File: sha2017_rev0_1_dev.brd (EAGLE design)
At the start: 65 x 80 mm, 87 parts, among them IC1 AP7215, IC2 LM1117, IC3 CP210X_USB_UART, IC4 ESP32WROOM32, Q1 MMBT2222A, Q2 MMBT2222A, Q3 SI1304 BDL, SW100 MCMT5-F-V, X701 2908-05WB-MG

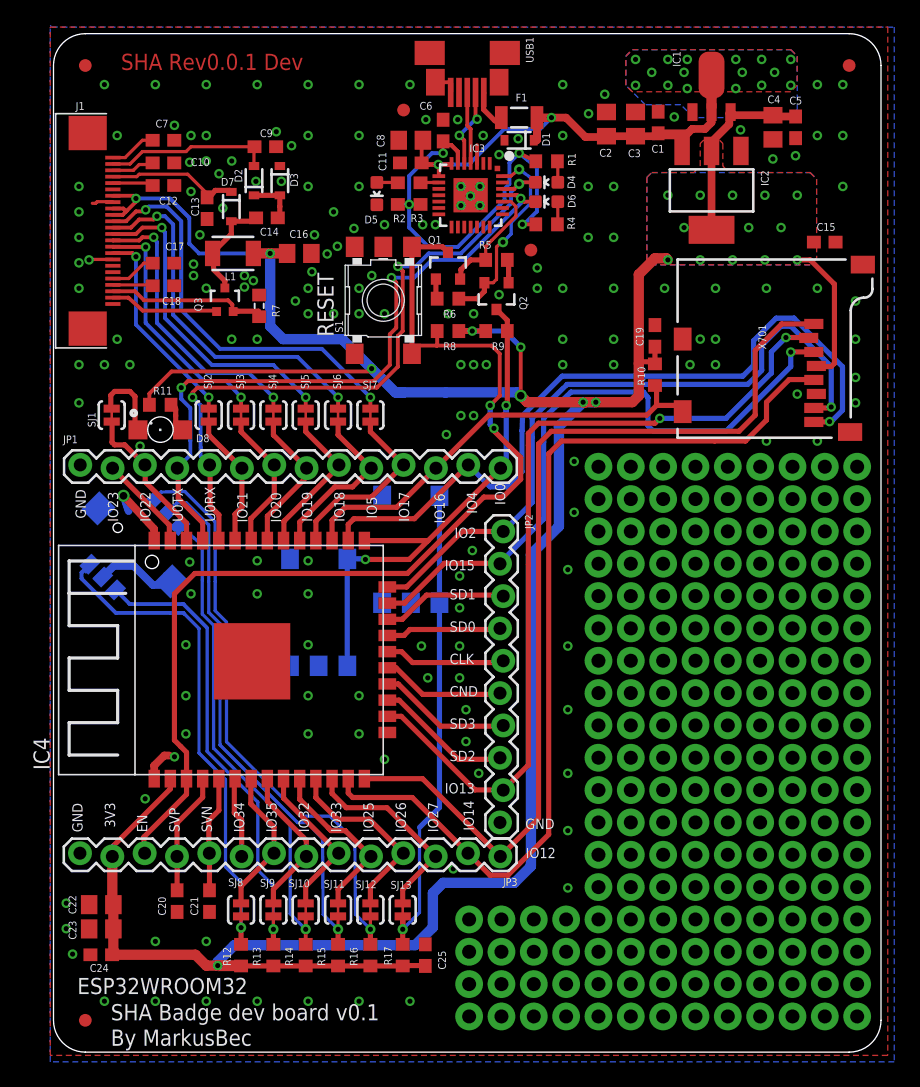
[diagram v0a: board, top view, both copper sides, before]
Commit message: added markings
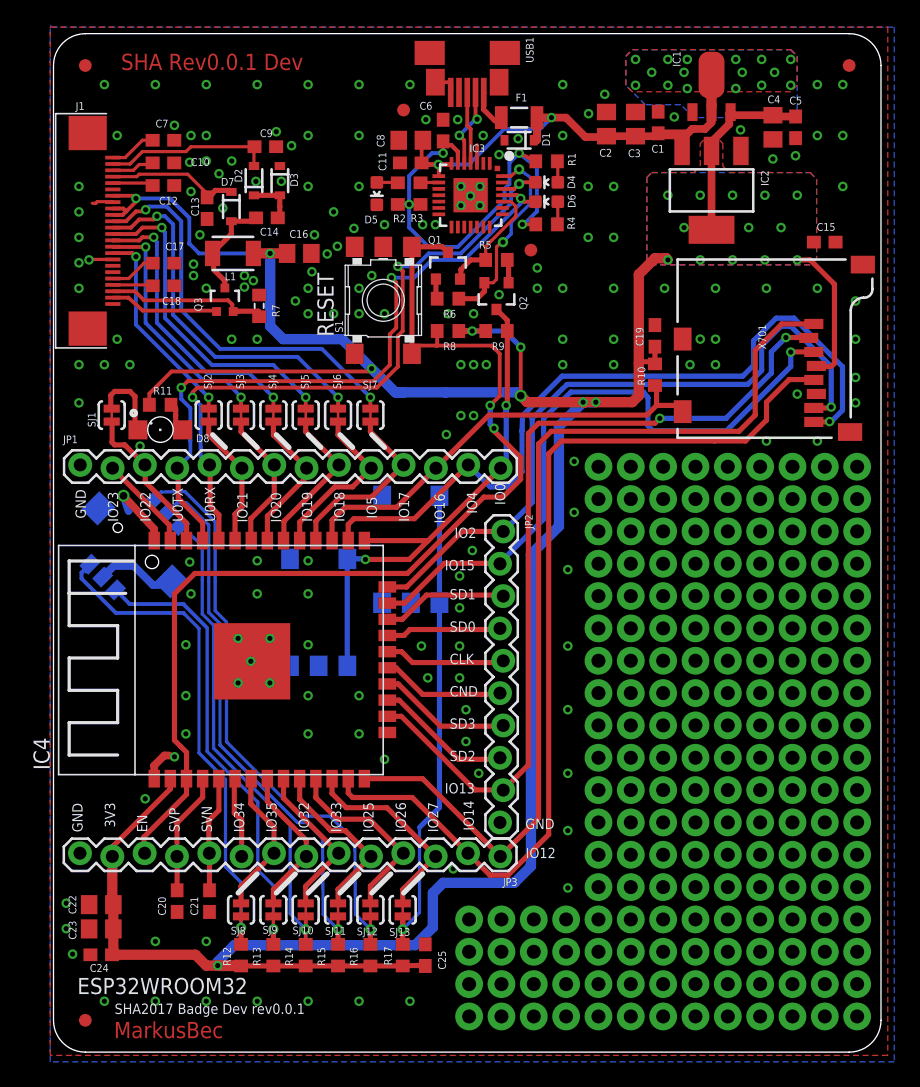
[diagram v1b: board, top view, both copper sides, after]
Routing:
- net GND: vias 171 -> 176
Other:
- board text added: "MarkusBec"
- board text added: "SHA2017 Badge Dev rev0.0.1"
- board text removed: "By MarkusBec"
- board text removed: "SHA Badge dev board v0.1"
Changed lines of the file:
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@@
 <?xml version="1.0" encoding="utf-8"?>
 <!DOCTYPE eagle SYSTEM "eagle.dtd">
-<eagle version="7.2.0">
+<eagle version="6.6.0">
 <drawing>
 <settings>
@@
 <setting verticaltext="up"/>
 </settings>
-<grid distance="0.5" unitdist="mm" unit="mm" style="lines" multiple="1" display="yes" altdistance="0.025" altunitdist="inch" altunit="inch"/>
+<grid distance="0.1" unitdist="mm" unit="mm" style="lines" multiple="1" display="yes" altdistance="0.025" altunitdist="inch" altunit="inch"/>
 <layers>
 <layer number="1" name="Top" color="4" fill="1" visible="yes" active="yes"/>
@@
 <layer number="60" name="bCarbon" color="7" fill="1" visible="no" active="no"/>
 <layer number="61" name="stand" color="7" fill="1" visible="no" active="no"/>
-<layer number="90" name="Modules" color="5" fill="1" visible="no" active="no"/>
+<layer number="90" name="Modules" color="5" fill="1" visible="no" active="yes"/>
 <layer number="91" name="Nets" color="2" fill="1" visible="no" active="no"/>
 <layer number="92" name="Busses" color="1" fill="1" visible="no" active="no"/>
@@
 <wire x1="2.5" y1="80" x2="0" y2="77.5" width="0" layer="20" curve="90"/>
 <wire x1="1.524" y1="50.038" x2="1.524" y2="79.248" width="0.4064" layer="22"/>
-<wire x1="1.524" y1="79.248" x2="63.246" y2="79.248" width="0.4064" layer="22"/>
-<wire x1="63.246" y1="79.248" x2="63.246" y2="50.038" width="0.4064" layer="22"/>
+<wire x1="1.524" y1="79.248" x2="9.906" y2="79.248" width="0.4064" layer="22"/>
+<wire x1="9.906" y1="79.248" x2="63.246" y2="79.248" width="0.4064" layer="22"/>
+<wire x1="63.246" y1="79.248" x2="63.246" y2="55.626" width="0.4064" layer="22"/>
+<wire x1="63.246" y1="55.626" x2="63.246" y2="50.038" width="0.4064" layer="22"/>
 <wire x1="63.246" y1="50.038" x2="1.524" y2="50.038" width="0.4064" layer="22"/>
 <polygon width="0.3048" layer="42">
@@
 <vertex x="0.127" y="17.018"/>
 </polygon>
-<text x="5.3" y="77.15" size="1.27" layer="1" font="vector" ratio="12">SHA Rev0.0.1 Dev</text>
+<text x="5.3" y="77.15" size="1.27" layer="1" font="vector" ratio="15">SHA Rev0.0.1 Dev</text>
+<text x="4.75" y="1.1" size="1.27" layer="1" font="vector" ratio="15">MarkusBec</text>
 <text x="2.286" y="17.272" size="0.8128" layer="25" font="vector" ratio="12" rot="R90">GND</text>
 <text x="7.366" y="17.272" size="0.8128" layer="25" font="vector" ratio="12" rot="R90">EN</text>
@@
 <text x="21.3" y="38.2" size="1.27" layer="26" font="vector" ratio="11" rot="MR0">A</text>
 <text x="24.6" y="34.6" size="0.6096" layer="26" font="vector" ratio="11" rot="MR270">FLASH</text>
-<text x="4.5" y="2.5" size="1.27" layer="25" font="vector" ratio="10">SHA Badge dev board v0.1</text>
-<text x="4.5" y="0.5" size="1.27" layer="25" font="vector" ratio="10">By MarkusBec</text>
+<wire x1="12.5" y1="48.5" x2="13.5" y2="47.5" width="0.4064" layer="25"/>
+<wire x1="15" y1="48.5" x2="16" y2="47.5" width="0.4064" layer="25"/>
+<wire x1="17.5" y1="48.5" x2="18.5" y2="47.5" width="0.4064" layer="25"/>
+<wire x1="20" y1="48.5" x2="21" y2="47.5" width="0.4064" layer="25"/>
+<wire x1="22.5" y1="48.5" x2="23.5" y2="47.5" width="0.4064" layer="25"/>
+<wire x1="25" y1="48.5" x2="26" y2="47.5" width="0.4064" layer="25"/>
+<wire x1="14.5" y1="12.5" x2="16" y2="14" width="0.4064" layer="25"/>
+<wire x1="17.5" y1="12.5" x2="19" y2="14" width="0.4064" layer="25"/>
+<wire x1="20" y1="12.5" x2="21.5" y2="14" width="0.4064" layer="25"/>
+<wire x1="22.5" y1="12.5" x2="24" y2="14" width="0.4064" layer="25"/>
+<wire x1="25" y1="12.5" x2="26.5" y2="14" width="0.4064" layer="25"/>
+<wire x1="27.5" y1="12.5" x2="29" y2="14" width="0.4064" layer="25"/>
+<text x="4.8" y="3" size="0.8128" layer="25" font="vector" ratio="15">SHA2017 Badge Dev rev0.0.1</text>
+<text x="4.75" y="1.1" size="1.27" layer="29" font="vector" ratio="15">MarkusBec</text>
 </plain>
 <attributes>
@@
 <pass name="Default">
 <param name="RoutingGrid" value="50mil"/>
-<param name="AutoGrid" value="1"/>
-<param name="Efforts" value="0"/>
-<param name="TopRouterVariant" value="1"/>
 <param name="tpViaShape" value="round"/>
 <param name="PrefDir.1" value="|"/>
@@
 </element>
 <element name="SJ8" library="SparkFun-Passives" package="PAD-JUMPER-2-NC_BY_TRACE_YES_SILK" value="JUMPER-PAD-2-NC_BY_TRACE" x="14.732" y="11.176" smashed="yes" rot="R90">
-<attribute name="NAME" x="13.7235" y="13.038" size="0.6096" layer="25" font="vector" ratio="12"/>
+<attribute name="NAME" x="13.9235" y="9.238" size="0.6096" layer="25" font="vector" ratio="12"/>
 <attribute name="VALUE" x="16.383" y="10.2235" size="0.4064" layer="27" rot="R90"/>
 </element>
 <element name="SJ9" library="SparkFun-Passives" package="PAD-JUMPER-2-NC_BY_TRACE_YES_SILK" value="JUMPER-PAD-2-NC_BY_TRACE" x="17.272" y="11.176" smashed="yes" rot="R90">
-<attribute name="NAME" x="16.2235" y="12.998" size="0.6096" layer="25" font="vector" ratio="12"/>
+<attribute name="NAME" x="16.4235" y="9.298" size="0.6096" layer="25" font="vector" ratio="12"/>
 <attribute name="VALUE" x="18.923" y="10.2235" size="0.4064" layer="27" rot="R90"/>
 </element>
 <element name="SJ10" library="SparkFun-Passives" package="PAD-JUMPER-2-NC_BY_TRACE_YES_SILK" value="JUMPER-PAD-2-NC_BY_TRACE" x="19.812" y="11.176" smashed="yes" rot="R90">
-<attribute name="NAME" x="18.4735" y="12.958" size="0.6096" layer="25" font="vector" ratio="12"/>
+<attribute name="NAME" x="18.7735" y="9.258" size="0.6096" layer="25" font="vector" ratio="12"/>
 <attribute name="VALUE" x="21.463" y="10.2235" size="0.4064" layer="27" rot="R90"/>
 </element>
 <element name="SJ12" library="SparkFun-Passives" package="PAD-JUMPER-2-NC_BY_TRACE_YES_SILK" value="JUMPER-PAD-2-NC_BY_TRACE" x="24.892" y="11.176" smashed="yes" rot="R90">
-<attribute name="NAME" x="23.7235" y="12.878" size="0.6096" layer="25" font="vector" ratio="12"/>
+<attribute name="NAME" x="23.8235" y="9.178" size="0.6096" layer="25" font="vector" ratio="12"/>
 <attribute name="VALUE" x="26.543" y="10.2235" size="0.4064" layer="27" rot="R90"/>
 </element>
 <element name="SJ11" library="SparkFun-Passives" package="PAD-JUMPER-2-NC_BY_TRACE_YES_SILK" value="JUMPER-PAD-2-NC_BY_TRACE" x="22.352" y="11.176" smashed="yes" rot="R90">
-<attribute name="NAME" x="21.2235" y="12.918" size="0.6096" layer="25" font="vector" ratio="12"/>
+<attribute name="NAME" x="21.3235" y="9.218" size="0.6096" layer="25" font="vector" ratio="12"/>
 <attribute name="VALUE" x="24.003" y="10.2235" size="0.4064" layer="27" rot="R90"/>
 </element>
 <element name="SJ13" library="SparkFun-Passives" package="PAD-JUMPER-2-NC_BY_TRACE_YES_SILK" value="JUMPER-PAD-2-NC_BY_TRACE" x="27.432" y="11.176" smashed="yes" rot="R90">
-<attribute name="NAME" x="26.4735" y="12.838" size="0.6096" layer="25" font="vector" ratio="12"/>
+<attribute name="NAME" x="26.3735" y="9.138" size="0.6096" layer="25" font="vector" ratio="12"/>
 <attribute name="VALUE" x="29.083" y="10.2235" size="0.4064" layer="27" rot="R90"/>
 </element>
@@
 <attribute name="VALUE" x="54.102" y="57.15" size="0.8128" layer="27" rot="R270"/>
 <attribute name="PARTNO" value="2908-05WB-MG" x="49.022" y="48.26" size="1.778" layer="27" rot="R270" display="off"/>
+<variant name="PRODUCTION" populate="no"/>
 </element>
 <element name="R10" library="rcl" package="R0603" value="100k" x="47.244" y="53.213" smashed="yes" rot="R270">
@@
 <element name="IC4" library="ESP3x" package="ESP32MOD" value="ESP32WROOM32" x="27.9" y="20.8" smashed="yes" rot="R90">
 <attribute name="NAME" x="-0.3" y="22.16" size="1.27" layer="25" rot="R90"/>
-<attribute name="VALUE" x="1.87" y="4.56" size="1.27" layer="25" font="vector"/>
+<attribute name="VALUE" x="1.87" y="4.56" size="1.27" layer="25" font="vector" ratio="15"/>
 </element>
 <element name="JP2" library="SparkFun-Connectors" package="1X10_LOCK" value="M10LOCK" x="35.2" y="40.9" smashed="yes" rot="R270">
@@
 <via x="1" y="9.7" extent="1-16" drill="0.4" diameter="0.6096"/>
 <via x="1" y="11.7" extent="1-16" drill="0.4" diameter="0.6096"/>
+<via x="14.5" y="32.5" extent="1-16" drill="0.4" diameter="0.6096"/>
+<via x="17" y="32.5" extent="1-16" drill="0.4" diameter="0.6096"/>
+<via x="15.5" y="30.7" extent="1-16" drill="0.4" diameter="0.6096"/>
+<via x="14.5" y="29" extent="1-16" drill="0.4" diameter="0.6096"/>
+<via x="17" y="29" extent="1-16" drill="0.4" diameter="0.6096"/>
 </signal>
 <signal name="USB_DN_CON">

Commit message: Swapped NC and IO23
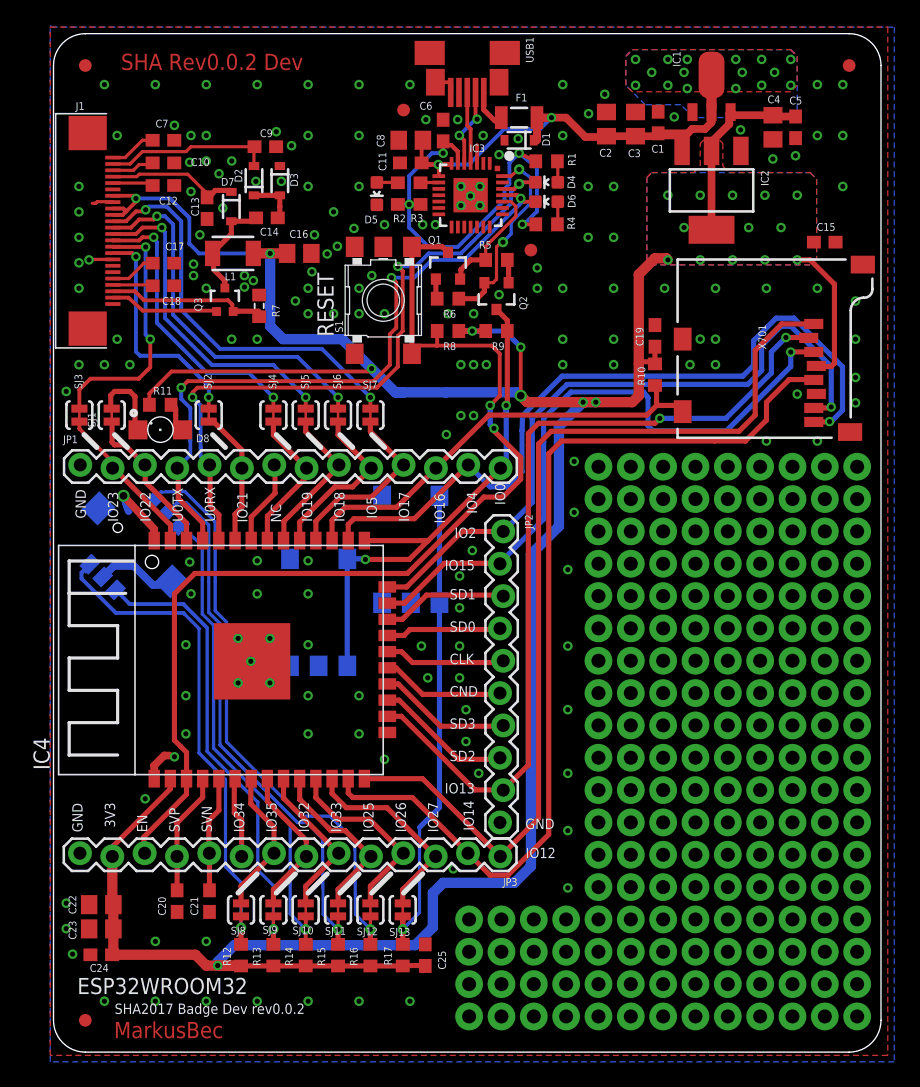
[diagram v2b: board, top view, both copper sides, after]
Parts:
- moved SJ3 12.7 mm to (2.03, 50.0)
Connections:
- removed net N$18: IC4.32, JP1.7, SJ3.1
- new net N$2: IC4.37, JP1.2, SJ3.1
- net N$15: now also IC4.32, JP1.7; no longer IC4.37, JP1.2
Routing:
- net N$2: track 0.00 -> 12.4 mm
- net N$18: track 11.2 -> 0.00 mm
- net LCD_BUSY: track 16.2 -> 18.0 mm
- net N$15: track 7.57 -> 6.75 mm
- net LCD_!RESET: track 19.4 -> 20.0 mm
- net GND: vias 176 -> 175
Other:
- board text added: "NC"
- board text added: "SHA Rev0.0.2 Dev"
- board text added: "SHA2017 Badge Dev rev0.0.2"
- board text removed: "IO20"
- board text removed: "SHA Rev0.0.1 Dev"
- board text removed: "SHA2017 Badge Dev rev0.0.1"
